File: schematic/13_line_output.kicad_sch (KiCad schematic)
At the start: 21 parts, among them J601 3.5mm mono line out, SW601 saw / pulse, U603 TL074HIDR

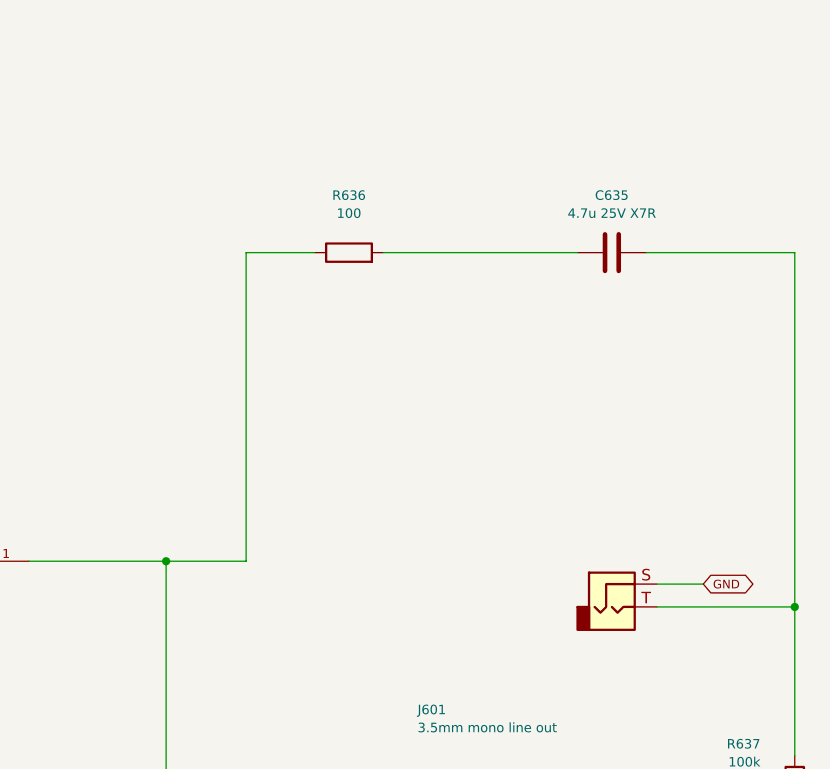
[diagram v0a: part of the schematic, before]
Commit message: add power supply, rail checks and parts list
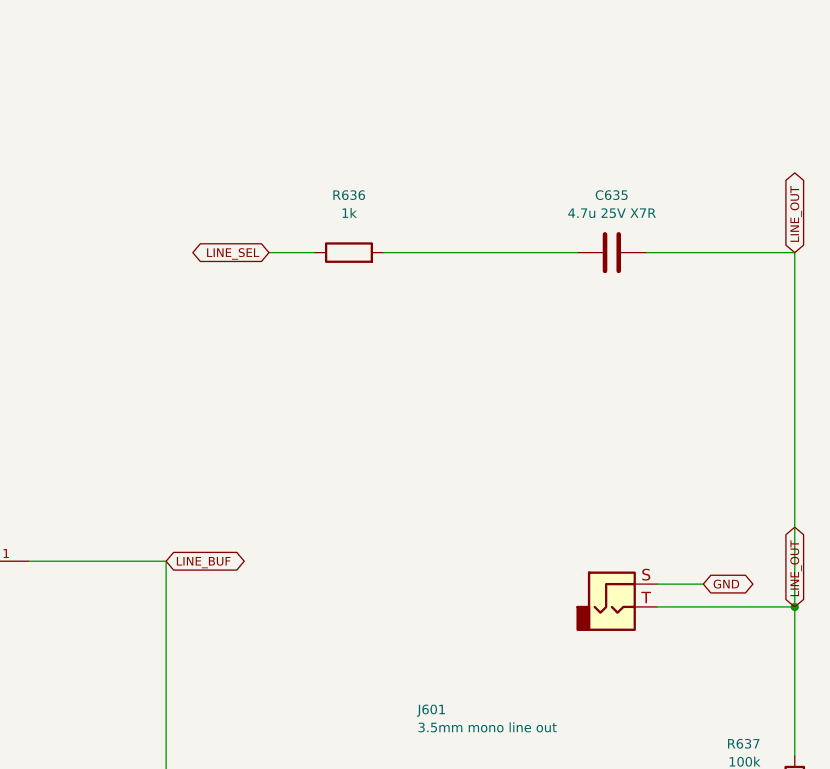
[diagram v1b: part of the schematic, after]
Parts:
- R636: value 100 -> 1k
- RV606: footprint (none) -> Potentiometer_THT:Potentiometer_Bourns_3296W_Vertical; MPN (none) -> 3296W-1-104LF; Manufacturer (none) -> Bourns; Supplier (none) -> LCSC
- U603: MPN (none) -> TL074HIDR; Manufacturer (none) -> Texas Instruments; Supplier (none) -> LCSC
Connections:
- net LINE_OUT: now reaches C635.2, J601.T, R637.1
- net LINE_BUF: now reaches U603.1 (OUT), U603.2 (-)
- net LINE_BUF: no longer R636.1
- new net LINE_SEL: R636.1
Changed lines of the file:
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@@
+      )
+    )
+    (property "MPN" "TL074HIDR"
+      (at 304.8 199.39 0.0)
+      (effects
+        (font
+          (size 1.0 1.0)
+        )
+        (hide yes)
+      )
+    )
+    (property "Manufacturer" "Texas Instruments"
+      (at 304.8 199.39 0.0)
+      (effects
+        (font
+          (size 1.0 1.0)
+        )
+        (hide yes)
+      )
+    )
+    (property "Supplier" "LCSC"
+      (at 304.8 199.39 0.0)
+      (effects
+        (font
+          (size 1.0 1.0)
+        )
+        (hide yes)
       )
     )
@@
         (font
           (size 1.05 1.05)
+        )
+        (hide yes)
+      )
+    )
+    (property "MPN" "TL074HIDR"
+      (at 90.17 250.19 0.0)
+      (effects
+        (font
+          (size 1.0 1.0)
+        )
+        (hide yes)
+      )
+    )
+    (property "Manufacturer" "Texas Instruments"
+      (at 90.17 250.19 0.0)
+      (effects
+        (font
+          (size 1.0 1.0)
+        )
+        (hide yes)
+      )
+    )
+    (property "Supplier" "LCSC"
+      (at 90.17 250.19 0.0)
+      (effects
+        (font
+          (size 1.0 1.0)
         )
         (hide yes)
@@
       )
     )
+    (property "MPN" "TL074HIDR"
+      (at 224.79 250.19 0.0)
+      (effects
+        (font
+          (size 1.0 1.0)
+        )
+        (hide yes)
+      )
+    )
+    (property "Manufacturer" "Texas Instruments"
+      (at 224.79 250.19 0.0)
+      (effects
+        (font
+          (size 1.0 1.0)
+        )
+        (hide yes)
+      )
+    )
+    (property "Supplier" "LCSC"
+      (at 224.79 250.19 0.0)
+      (effects
+        (font
+          (size 1.0 1.0)
+        )
+        (hide yes)
+      )
+    )
     (instances
       (project "arpeggiator"
@@
       )
     )
+    (property "MPN" "TL074HIDR"
+      (at 355.6 250.19 0.0)
+      (effects
+        (font
+          (size 1.0 1.0)
+        )
+        (hide yes)
+      )
+    )
+    (property "Manufacturer" "Texas Instruments"
+      (at 355.6 250.19 0.0)
+      (effects
+        (font
+          (size 1.0 1.0)
+        )
+        (hide yes)
+      )
+    )
+    (property "Supplier" "LCSC"
+      (at 355.6 250.19 0.0)
+      (effects
+        (font
+          (size 1.0 1.0)
+        )
+        (hide yes)
+      )
+    )
     (instances
       (project "arpeggiator"
@@
       )
     )
-    (property "Value" "100"
+    (property "Value" "1k"
       (at 350.52 160.75 90.0)
       (effects
@@
     )
   )
+  (wire
+    (pts
+      (xy 346.71 165.1)
+      (xy 341.63 165.1)
+    )
+    (stroke
+      (width 0)
+      (type default)
+    )
+  )
+  (global_label "LINE_SEL"
+    (shape bidirectional)
+    (at 341.63 165.1 180.0)
+    (effects
+      (font
+        (size 0.95 0.95)
+      )
+      (justify right)
+    )
+  )
   (symbol
     (lib_id "Device:C")
@@
     (on_board no)
     (dnp no)
-    (property "Reference" "#PWR21052"
+    (property "Reference" "#PWR21054"
       (at 400.05 233.68 0.0)
       (effects
@@
       (project "arpeggiator"
         (path "/b74f2899-8338-4c76-a1a7-8fd841787321/b5a5f94a-db0b-5750-bf2e-932028180051"
-          (reference "#PWR21052")
+          (reference "#PWR21054")
           (unit 1)
         )
@@
     (on_board no)
     (dnp no)
-    (property "Reference" "#PWR21059"
+    (property "Reference" "#PWR21061"
       (at 35.56 271.78 0.0)
       (effects
@@
       (project "arpeggiator"
         (path "/b74f2899-8338-4c76-a1a7-8fd841787321/b5a5f94a-db0b-5750-bf2e-932028180051"
-          (reference "#PWR21059")
+          (reference "#PWR21061")
           (unit 1)
         )
@@
     (on_board no)
     (dnp no)
-    (property "Reference" "#PWR21066"
+    (property "Reference" "#PWR21068"
       (at 165.1 259.08 0.0)
       (effects
@@
       (project "arpeggiator"
         (path "/b74f2899-8338-4c76-a1a7-8fd841787321/b5a5f94a-db0b-5750-bf2e-932028180051"
-          (reference "#PWR21066")
+          (reference "#PWR21068")
           (unit 1)
         )
@@
       )
     )
-    (property "Footprint" ""
+    (property "Footprint" "Potentiometer_THT:Potentiometer_Bourns_3296W_Vertical"
       (at 264.15999999999997 241.3 0.0)
       (effects
@@
       )
     )
-    (property "Datasheet" ""
+    (property "Datasheet" "https://www.bourns.com/docs/product-datasheets/3296.pdf"
       (at 264.15999999999997 241.3 0.0)
       (effects
@@
         )
         (justify left)
+        (hide yes)
+      )
+    )
+    (property "MPN" "3296W-1-104LF"
+      (at 294.64 250.19 0.0)
+      (effects
+        (font
+          (size 1.0 1.0)
+        )
+        (hide yes)
+      )
+    )
+    (property "Manufacturer" "Bourns"
+      (at 294.64 250.19 0.0)
+      (effects
+        (font
+          (size 1.0 1.0)
+        )
+        (hide yes)
+      )
+    )
+    (property "Supplier" "LCSC"
+      (at 294.64 250.19 0.0)
+      (effects
+        (font
+          (size 1.0 1.0)
+        )
         (hide yes)
       )
@@
     (on_board no)
     (dnp no)
-    (property "Reference" "#PWR21069"
+    (property "Reference" "#PWR21071"
       (at 294.64 241.3 0.0)
       (effects
@@
       (project "arpeggiator"
         (path "/b74f2899-8338-4c76-a1a7-8fd841787321/b5a5f94a-db0b-5750-bf2e-932028180051"
-          (reference "#PWR21069")
+          (reference "#PWR21071")
           (unit 1)
         )
@@
     )
   )
-  (wire
-    (pts
-      (xy 330.2 199.39)
-      (xy 339.09 199.39)
-    )
-    (stroke
-      (width 0)
-      (type default)
-    )
-  )
-  (wire
-    (pts
-      (xy 339.09 199.39)
-      (xy 339.09 165.1)
-    )
-    (stroke
-      (width 0)
-      (type default)
-    )
-  )
-  (wire
-    (pts
-      (xy 339.09 165.1)
-      (xy 346.71 165.1)
-    )
-    (stroke
-      (width 0)
-      (type default)
-    )
-  )
-  (junction
-    (at 330.2 199.39)
-    (diameter 0.0)
-    (color 0 0 0 0)
+  (global_label "LINE_BUF"
+    (shape bidirectional)
+    (at 330.2 199.39 0.0)
+    (effects
+      (font
+        (size 0.95 0.95)
+      )
+      (justify left)
+    )
   )
   (wire
@@
       (width 0)
       (type default)
+    )
+  )
+  (global_label "LINE_OUT"
+    (shape bidirectional)
+    (at 400.05 165.1 90.0)
+    (effects
+      (font
+        (size 0.95 0.95)
+      )
+      (justify left)
     )
   )
@@
     (color 0 0 0 0)
   )
-  (wire
+  (global_label "LINE_OUT"
+    (shape bidirectional)
+    (at 400.05 204.47 90.0)
+    (effects
+      (font
+        (size 0.95 0.95)
+      )
+      (justify left)
+    )
+  )
+  (wire

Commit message: pick controls and start pcb placement
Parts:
- C631, C632: value 100n film -> 100n film 100V 5%; footprint (none) -> Capacitor_THT:C_Rect_L7.2mm_W2.5mm_P5.00mm; MPN (none) -> R82EC3100DQ70J; Manufacturer (none) -> KEMET; Supplier (none) -> Tayda; Supplier URL (none) -> https://www.taydaelectronics.com/0-1uf-100v-5-kemet-polyest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
- C633: value 470n film -> 470n film 63V 5%; footprint (none) -> Capacitor_THT:C_Rect_L7.2mm_W3.5mm_P5.00mm; MPN (none) -> R82DC3470AA60J; Manufacturer (none) -> KEMET; Supplier (none) -> DigiKey; Supplier URL (none) -> https://www.digikey.com/en/products/detail/kemet/R82DC3470A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
- J601: footprint (none) -> Arpeggiator:Jack_PJ-3001F_Vertical; symbol Connector_Audio:AudioJack2 -> Connector_Audio:AudioJack2_SwitchT; MPN (none) -> PJ-3001F; Manufacturer (none) -> Tayda; Supplier (none) -> Tayda; Supplier URL (none) -> https://www.taydaelectronics.com/pj-3001f-3-5-mm-mono-phone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
- RV603, RV605: footprint (none) -> Potentiometer_THT:Potentiometer_Alpha_RD901F-40-00D_Single_Vertical; MPN (none) -> RD901F-40-15F-B100K; Manufacturer (none) -> Taiwan Alpha; Supplier (none) -> Tayda; Supplier URL (none) -> https://www.taydaelectronics.com/100k-ohm-linear-taper-pote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
- RV604: footprint (none) -> Potentiometer_THT:Potentiometer_Alpha_RD901F-40-00D_Single_Vertical; MPN (none) -> RD901F-40-15F-A100K; Manufacturer (none) -> Taiwan Alpha; Supplier (none) -> Tayda; Supplier URL (none) -> https://www.taydaelectronics.com/100k-ohm-logarithmic-taper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
- SW601: footprint (none) -> Arpeggiator:SW_Dailywell_1M_SPDT_M2; MPN (none) -> 1MS1T1B1M2QES; Manufacturer (none) -> Dailywell; Supplier (none) -> Tayda; Supplier URL (none) -> https://www.taydaelectronics.com/electromechanical/switches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
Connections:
- net GND: now also RV604.1, RV605.1; no longer RV604.3, RV605.3
- net REF2V5: now also RV605.3; no longer RV605.1
- net at C634.1, RV603.2: now also RV603.1, RV604.3; no longer RV603.3, RV604.1
- net at R635.2: now also RV603.3; no longer RV603.1
- no-connect marks 0 -> 1
